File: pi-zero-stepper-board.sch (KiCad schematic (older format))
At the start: 18 parts, among them CON1 DC12v, P1 Servo (A0), P2 Endstop1 (A1), P3 Endstop2 (A2), P4 Stepper1, P5 Stepper2, P6 COM, P7 Aux (D10 - 13), SW1 SW_PUSH, SW2 SPDT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

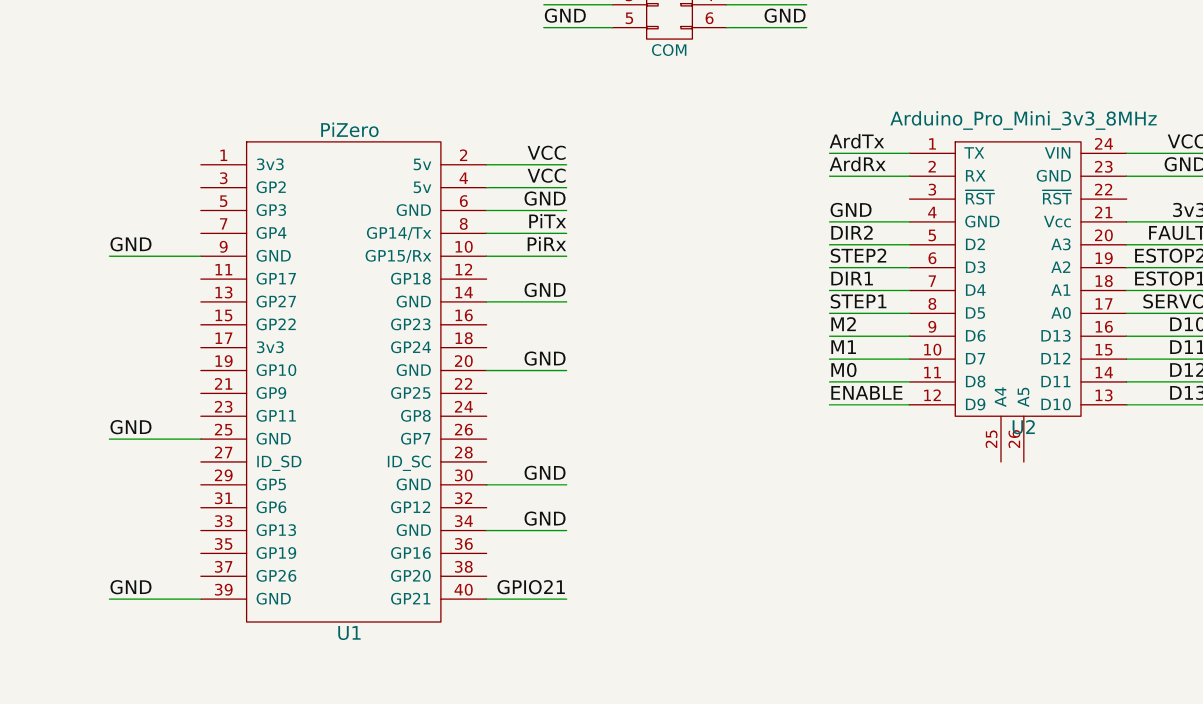
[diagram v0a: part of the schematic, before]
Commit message: Fixed power track, added I2C and updated brd text
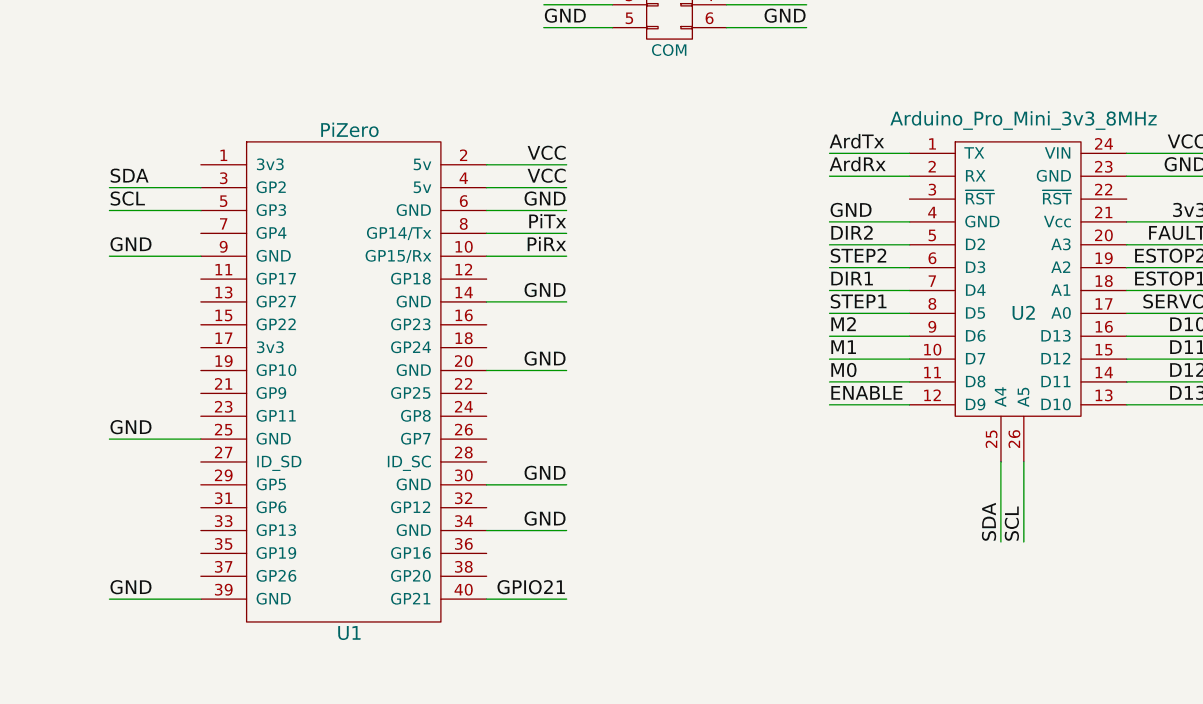
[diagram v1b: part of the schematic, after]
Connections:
- net SDA: now reaches U2.25 (A4)
- net SDA: now also U1.3 (GP2)
- net SCL: now reaches U2.26 (A5)
- net SCL: now also U1.5 (GP3)
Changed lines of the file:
@@
 U 1 1 56E571C7
 P 5200 3050
-F 0 "U2" H 5200 2400 60  0000 C CNN
+F 0 "U2" H 5200 2900 60  0000 C CNN
 F 1 "Arduino_Pro_Mini_3v3_8MHz" H 5200 3750 60  0000 C CNN
 F 2 "custom:Arduino_Pro_Mini" H 5200 2500 60  0001 C CNN
@@
 Text Label 3200 4450 2    60   ~ 0
 GPIO21
+Wire Wire Line
+	5100 3850 5100 4200
+Wire Wire Line
+	5200 3850 5200 4200
+Text Label 5100 4200 1    60   ~ 0
+SDA
+Text Label 5200 4200 1    60   ~ 0
+SCL
+Wire Wire Line
+	1600 2650 1200 2650
+Wire Wire Line
+	1600 2750 1200 2750
+Text Label 1200 2650 0    60   ~ 0
+SDA
+Text Label 1200 2750 0    60   ~ 0
+SCL
 $EndSCHEMATC

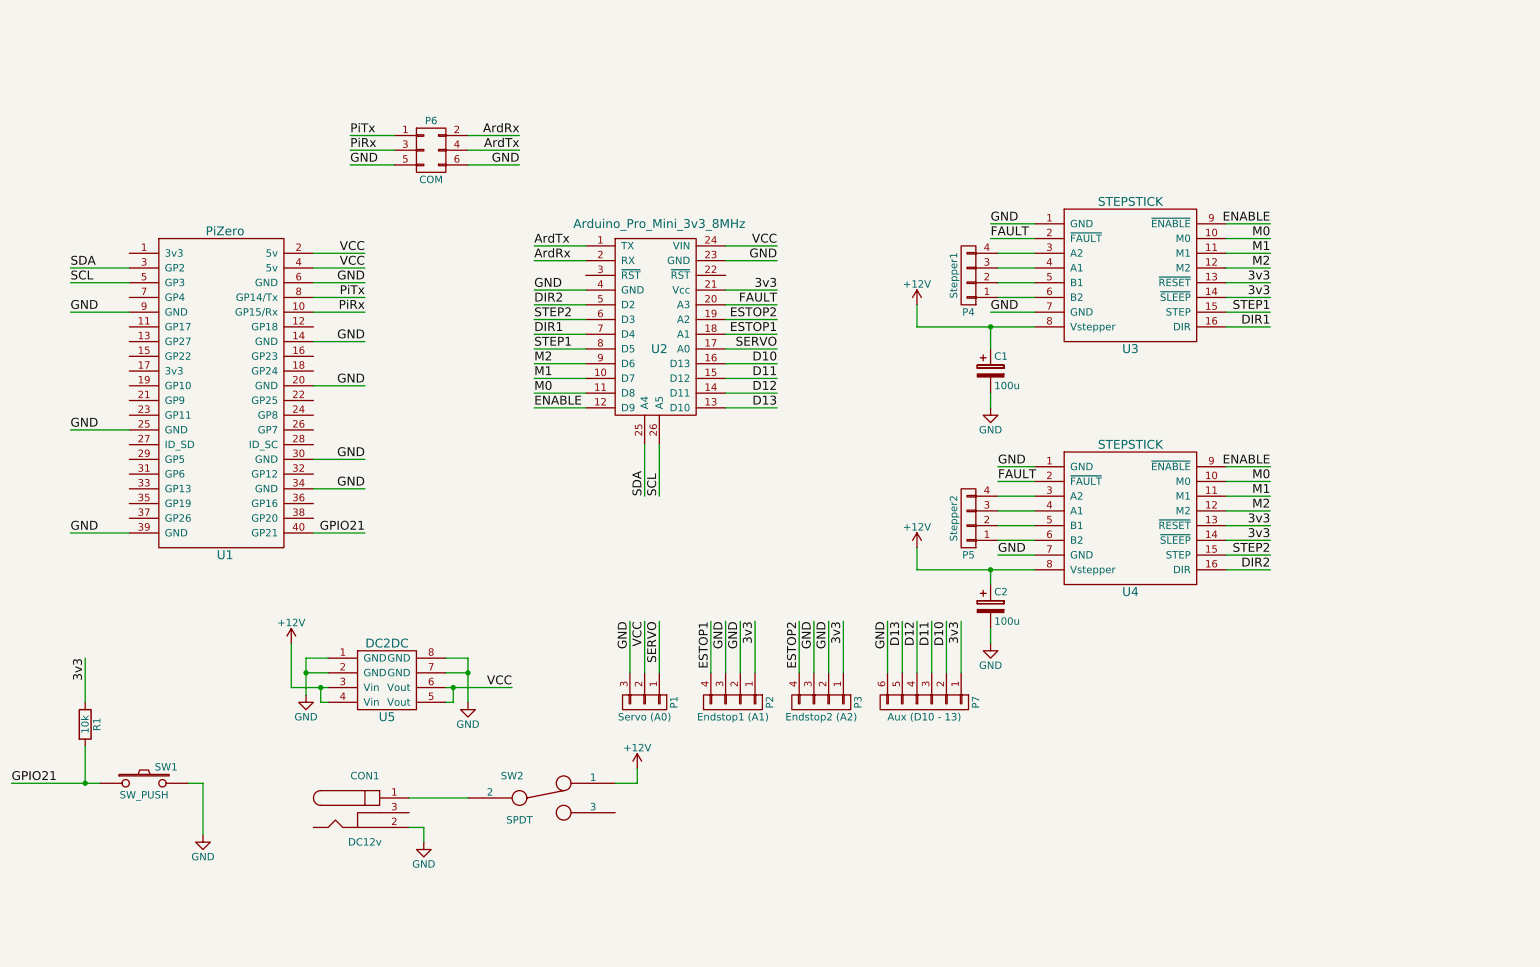
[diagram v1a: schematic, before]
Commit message: Added I2C and other fixes
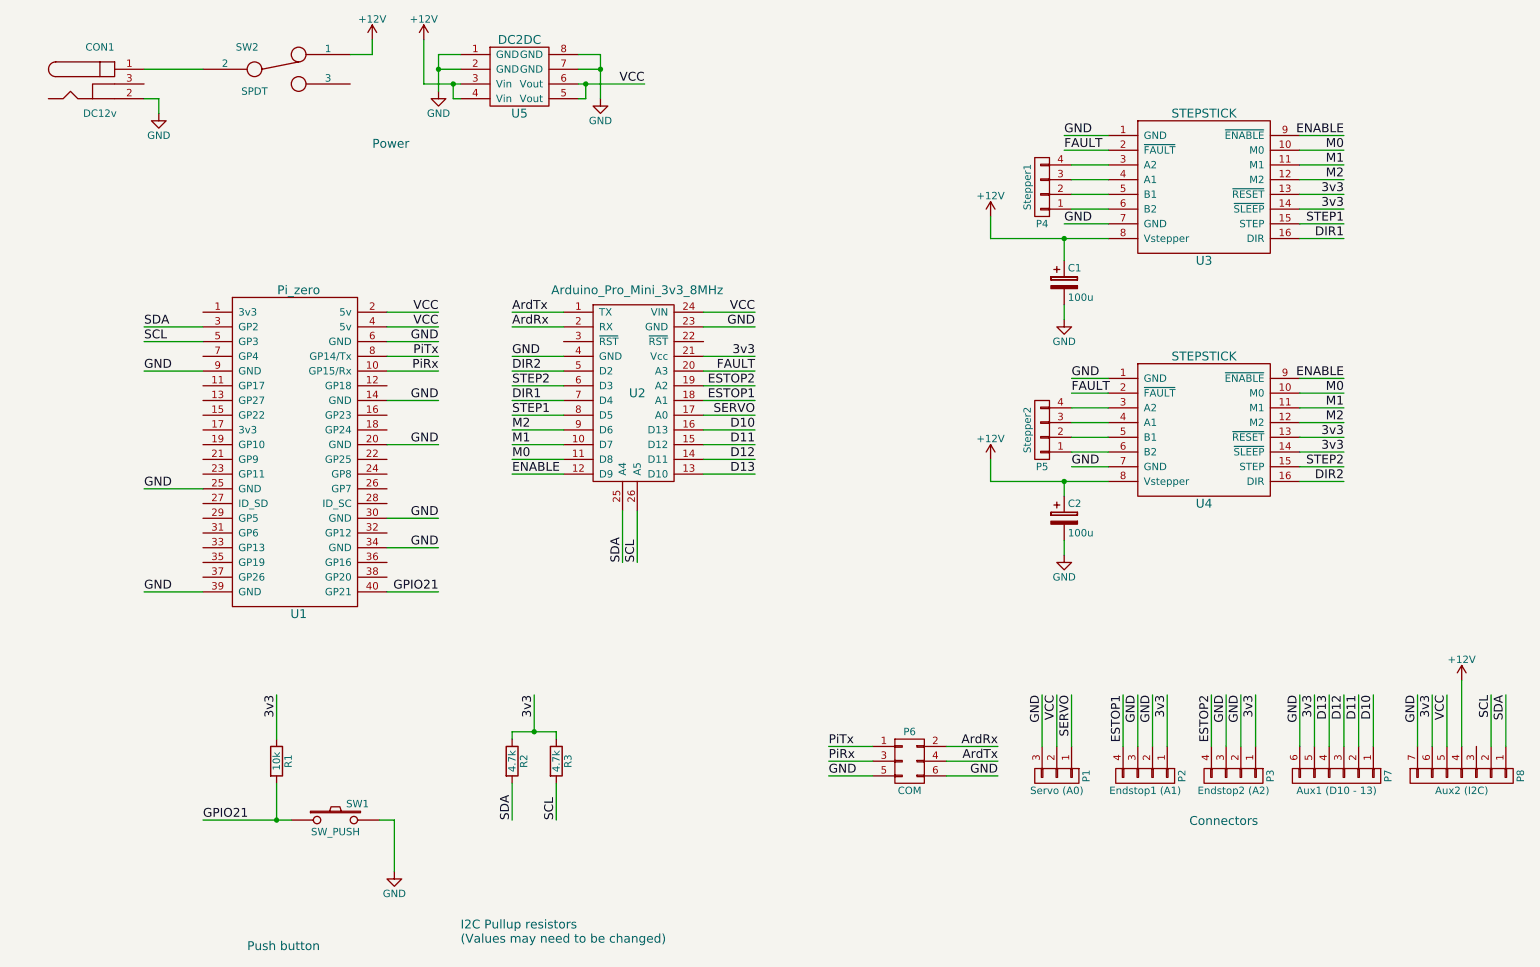
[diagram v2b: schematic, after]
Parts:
- removed U1: PiZero, custom:Pi_Zero, symbol PiZero
- added P8: Aux2 (I2C), Pin_Headers:Pin_Header_Straight_1x07, symbol CONN_01X07
- added R2, R3: 4.7k, Discret:R1, symbol R
- added U1: Pi_zero, custom:Pi_Zero, symbol Pi2_3_GPIO
- P7: value Aux (D10 - 13) -> Aux1 (D10 - 13)
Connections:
- net +12V: now also P8.4 (P4)
- net 3v3: now also P7.5 (P5), P8.6 (P6), R2.1, R3.1; no longer P7.1 (P1)
- net D10: now also P7.1 (P1); no longer P7.2 (P2)
- net D11: now also P7.2 (P2); no longer P7.3 (P3)
- net D12: now also P7.3 (P3); no longer P7.4 (P4)
- net D13: now also P7.4 (P4); no longer P7.5 (P5)
- net GND: now also P8.7 (P7), U1.14 (GND), U1.20 (GND), U1.25 (GND), U1.30 (GND), U1.34 (GND), U1.39 (GND), U1.6 (GND), U1.9 (GND)
- net GPIO21: now also U1.40 (GP21)
- net PiRx: now also U1.10 (GP15/Rx)
- net PiTx: now also U1.8 (GP14/Tx)
- net SCL: now also P8.2 (P2), R3.2, U1.5 (GP3)
- net SDA: now also P8.1 (P1), R2.2, U1.3 (GP2)
- net VCC: now also P8.5 (P5), U1.2 (5v), U1.4 (5v)
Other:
- note added: "Connectors"
- note added: "I2C Pullup resistors \n(Values may need to be changed)"
- note added: "Power"
- note added: "Push button"
- moved on the sheet: C1, C2, CON1, P1, P2, P3, P4, P5, P6, P7, R1, SW1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
